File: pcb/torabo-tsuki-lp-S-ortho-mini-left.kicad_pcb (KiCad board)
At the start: 2 copper layers, 128.5 x 74 mm, 55 parts, among them J101 FTSH-106-01-L-D-K, SW10 SW_Push, SW11 SW_Push, SW12 SW_Push, SW13 SW_Push, SW15 SW_Push, SW16 SW_Push, SW17 SW_Push, SW18 SW_Push, SW19 SW_Push, SW20 SW_Push, SW22 SW_Push, SW23 SW_Push, SW24 SW_Push, SW25 SW_Push, SW26 SW_Push, SW27 SW_Push, SW28 SW_Push, SW29 SW_Push, SW30 SW_Push, SW31 SW_Push, SW32 SW_Push, SW33 SW_Push, SW34 SW_Push, SW35 SW_Push, SW8 SW_Push, SW9 SW_Push

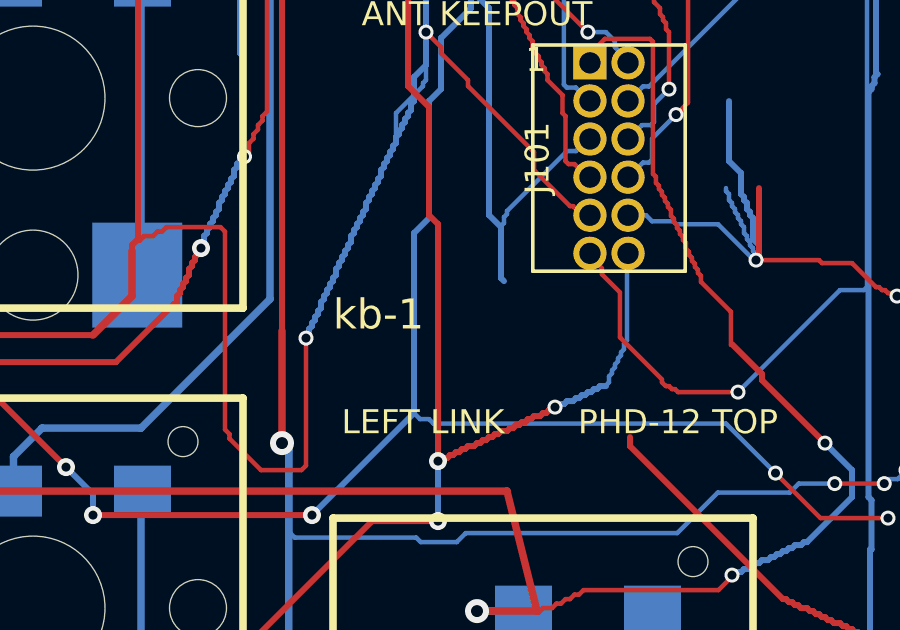
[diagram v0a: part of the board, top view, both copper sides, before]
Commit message: Rename keyboard to FORT-48
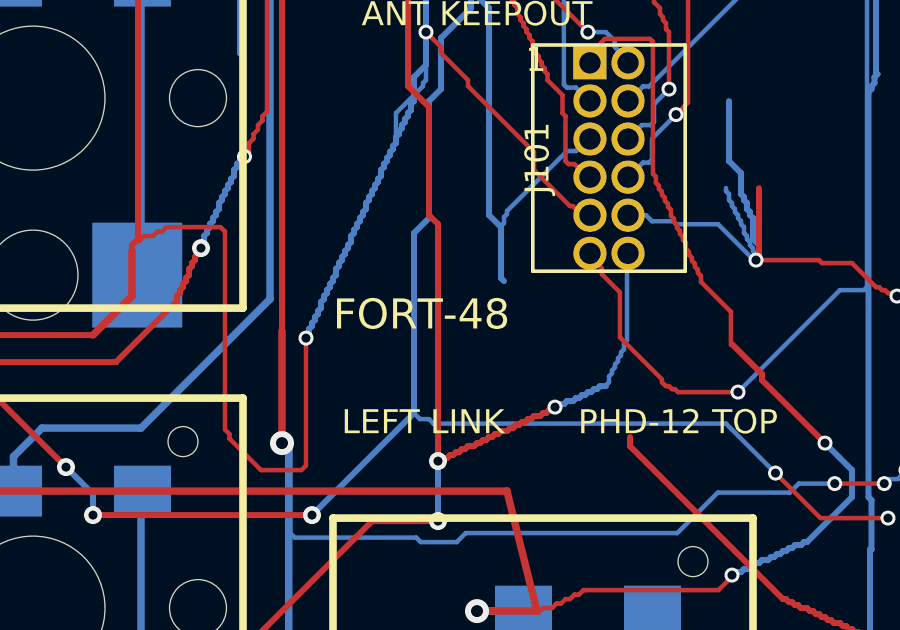
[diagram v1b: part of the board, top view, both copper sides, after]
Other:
- board text added: "FORT-48"
- board text removed: "kb-1"
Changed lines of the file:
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@@
 		)
 	)
-	(gr_text "kb-1"
+	(gr_text "FORT-48"
 		(at 114 75.8 0)
 		(layer "F.SilkS")

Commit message: Rename keyboard to komoro (#54)
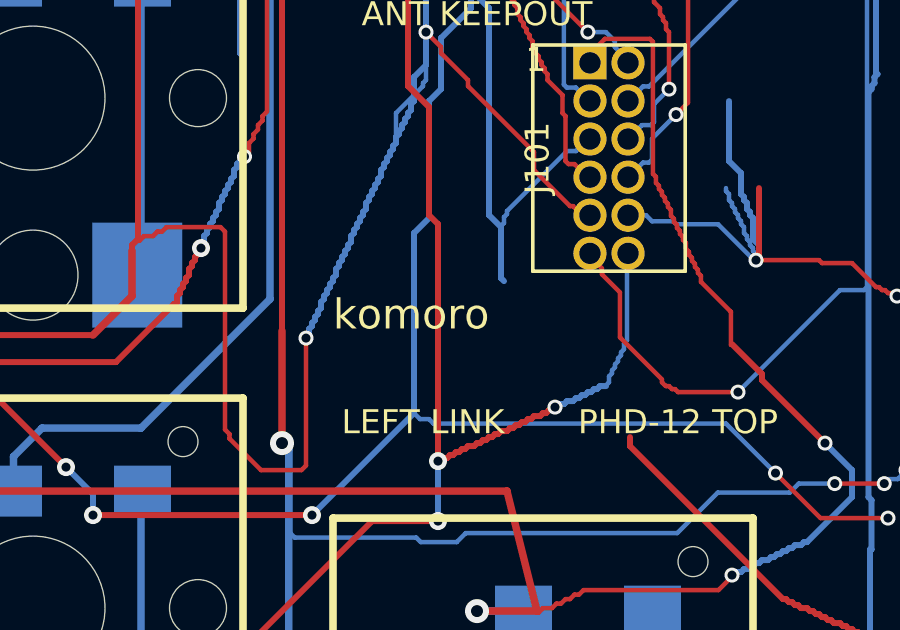
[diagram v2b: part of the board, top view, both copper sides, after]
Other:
- board text added: "komoro"
- board text removed: "FORT-48"
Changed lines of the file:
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@@
 		)
 	)
-	(gr_text "FORT-48"
+	(gr_text "komoro"
 		(at 114 75.8 0)
 		(layer "F.SilkS")

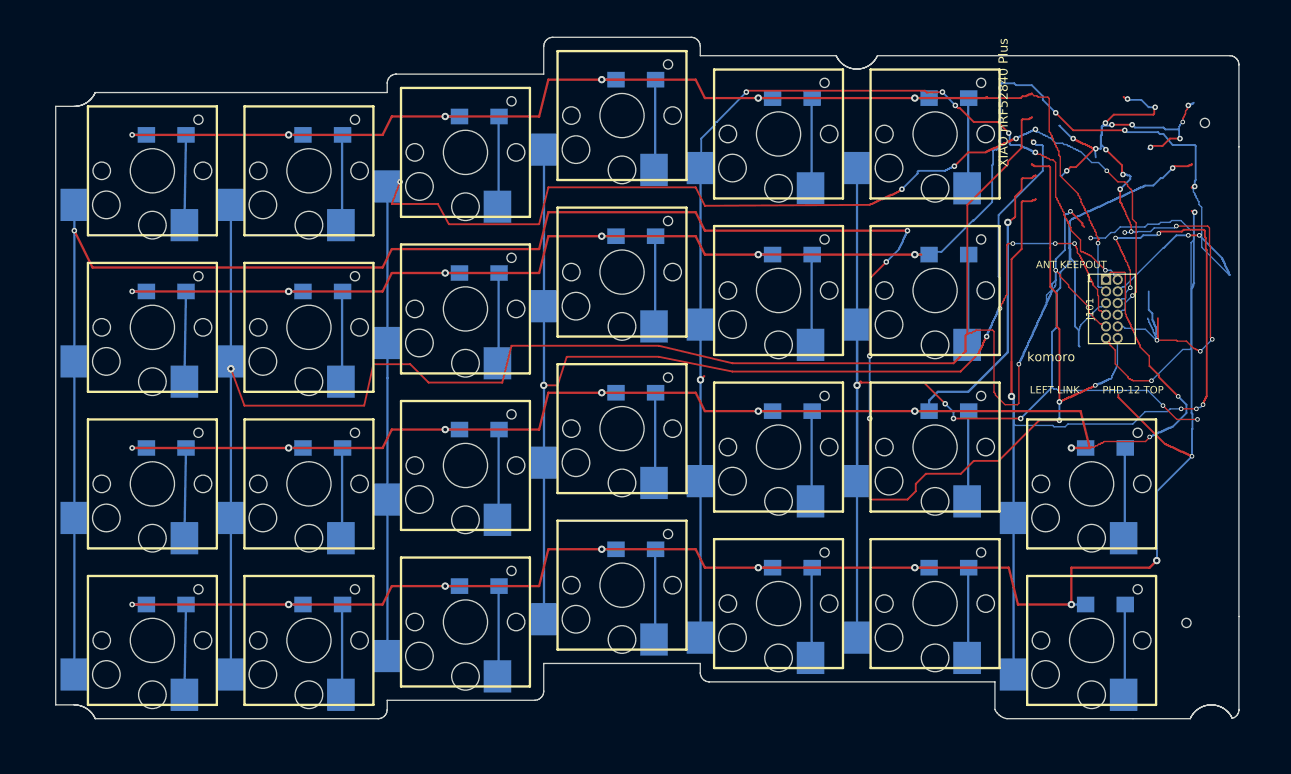
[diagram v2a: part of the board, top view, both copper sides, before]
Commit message: Expand PCB screw reliefs by 0.35 mm (#60)
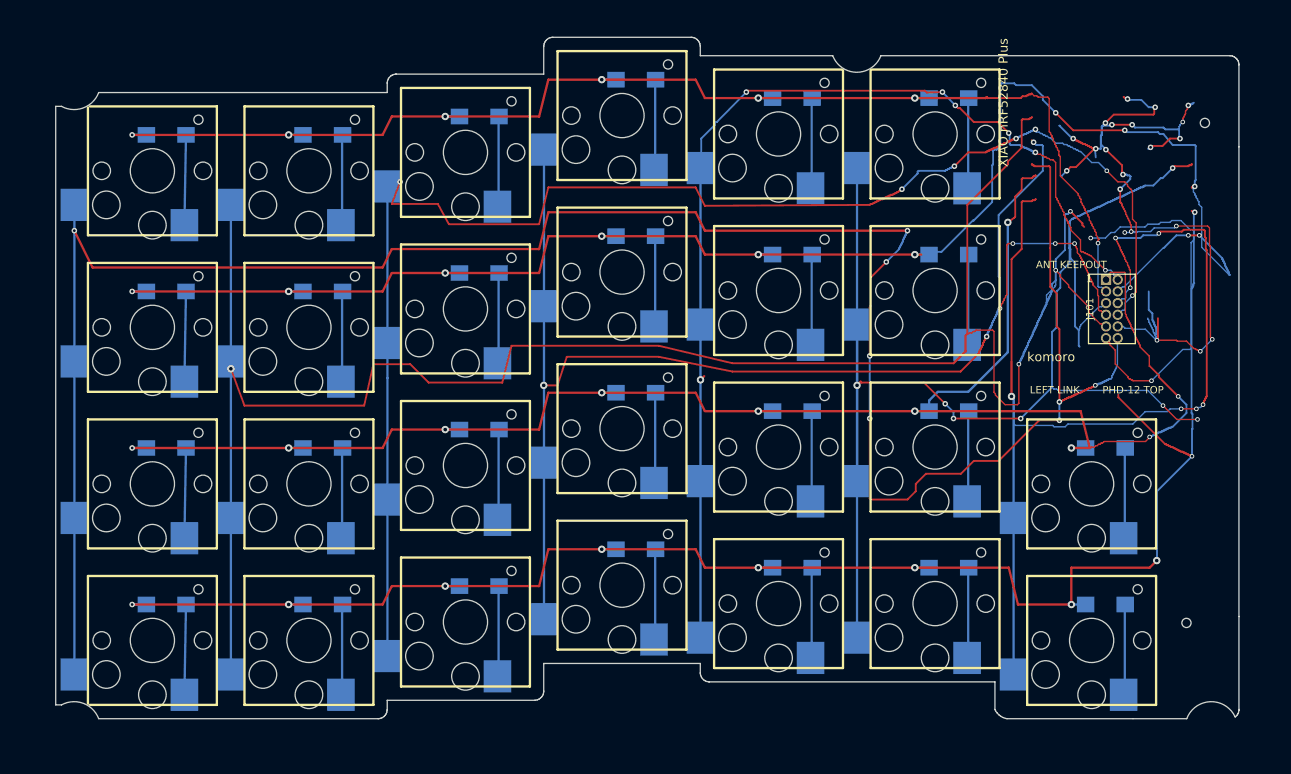
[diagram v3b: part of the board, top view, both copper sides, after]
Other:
- outline, holes or cut-outs redrawn
